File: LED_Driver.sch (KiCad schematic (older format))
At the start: 0 parts

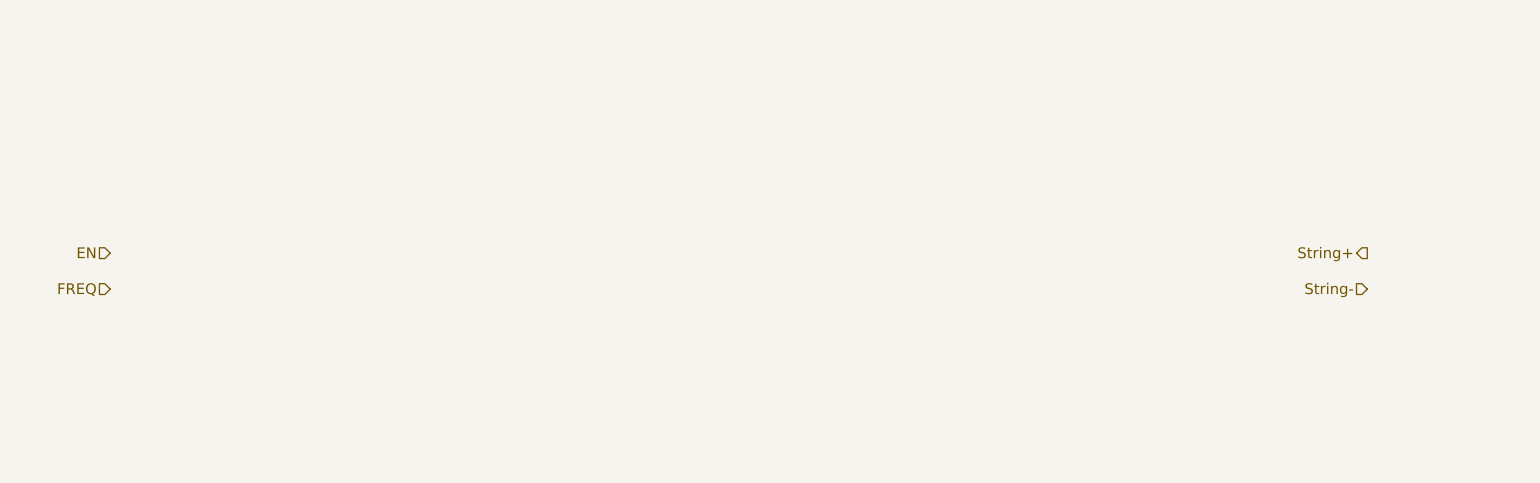
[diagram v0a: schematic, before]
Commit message: Rough schematic created for LED driver circuit
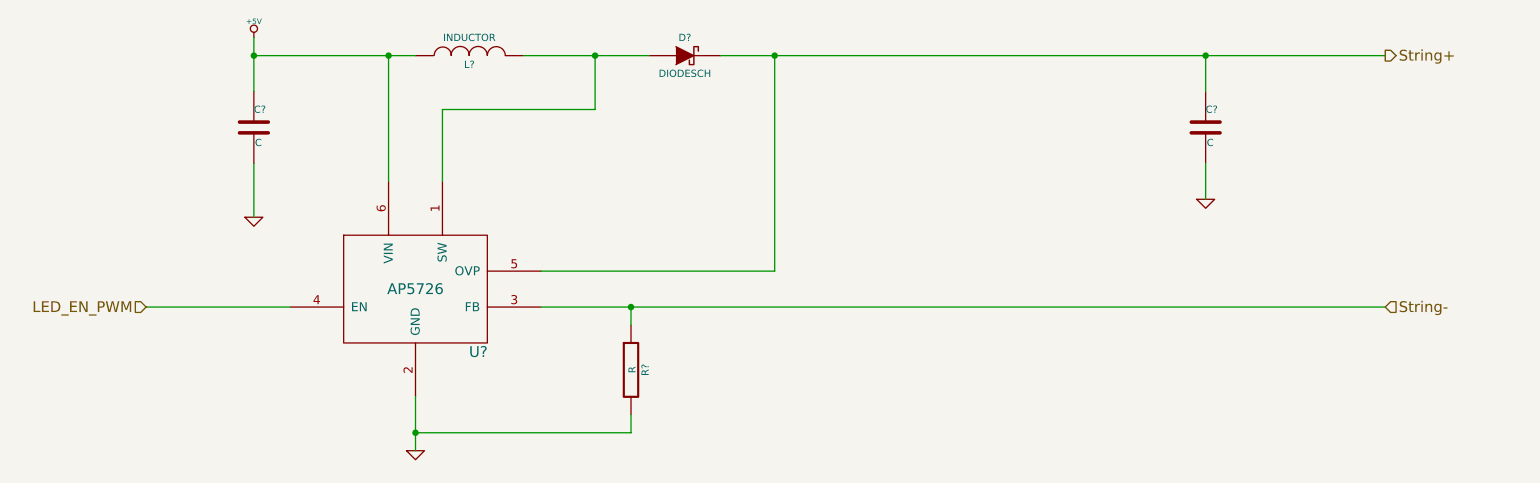
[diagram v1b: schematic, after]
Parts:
- added C? (x2): C, symbol C
- added D?: DIODESCH, symbol DIODESCH
- added L?: INDUCTOR, symbol INDUCTOR
- added R?: R, symbol R
- added U?: AP5726, symbol AP5726
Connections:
- net String+: now also C?.1, D?.2 (K), U?.5 (OVP)
- net String-: now also R?.1, U?.3 (FB)
- new net: D?.1 (A), L?.2, U?.1 (SW)
- new net +5V: C?.1, L?.1, U?.6 (VIN)
- new net GND: C?.2, C?.2, R?.2, U?.2 (GND)
- new net LED_EN_PWM: U?.4 (EN)
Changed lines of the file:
@@
 $Descr A4 11693 8268
 encoding utf-8
-Sheet 5 9
+Sheet 4 9
 Title ""
 Date ""
@@
 Comment4 ""
 $EndDescr
-Text HLabel 2400 2100 0    60   Input ~ 0
-EN
-Text HLabel 2400 2300 0    60   Input ~ 0
-FREQ
-Text HLabel 9400 2100 0    60   Output ~ 0
+Text HLabel 2600 2400 0    60   Input ~ 0
+LED_EN_PWM
+Text HLabel 9500 1000 2    60   Output ~ 0
 String+
-Text HLabel 9400 2300 0    60   Input ~ 0
+Text HLabel 9500 2400 2    60   Input ~ 0
 String-
+Wire Wire Line
+	2600 2400 3400 2400
+$Comp
+L AP5726 U?
+U 1 1 52F2B7AF
+P 4100 2300
+F 0 "U?" H 4450 1950 60  0000 C CNN
+F 1 "AP5726" H 4100 2300 60  0000 C CNN
+F 2 "" H 4100 2300 60  0000 C CNN
+F 3 "" H 4100 2300 60  0000 C CNN
+	1    4100 2300
+	1    0    0    -1
+$EndComp
+$Comp
+L +5V #PWR?
+U 1 1 52F2BDD5
+P 3200 900
+F 0 "#PWR?" H 3200 990 20  0001 C CNN
+F 1 "+5V" H 3200 990 30  0000 C CNN
+F 2 "" H 3200 900 60  0000 C CNN
+F 3 "" H 3200 900 60  0000 C CNN
+	1    3200 900
+	1    0    0    -1
+$EndComp
+$Comp
+L GND #PWR?
+U 1 1 52F2BDE9
+P 3200 1900
+F 0 "#PWR?" H 3200 1900 30  0001 C CNN
+F 1 "GND" H 3200 1830 30  0001 C CNN
+F 2 "" H 3200 1900 60  0000 C CNN
+F 3 "" H 3200 1900 60  0000 C CNN
+	1    3200 1900
+	1    0    0    -1
+$EndComp
+$Comp
+L GND #PWR?
+U 1 1 52F2BDFB
+P 4100 3200
+F 0 "#PWR?" H 4100 3200 30  0001 C CNN
+F 1 "GND" H 4100 3130 30  0001 C CNN
+F 2 "" H 4100 3200 60  0000 C CNN
+F 3 "" H 4100 3200 60  0000 C CNN
+	1    4100 3200
+	1    0    0    -1
+$EndComp
+Wire Wire Line
+	4100 3200 4100 2900
+$Comp
+L C C?
+U 1 1 52F2BE0B
+P 3200 1400
+F 0 "C?" H 3200 1500 40  0000 L CNN
+F 1 "C" H 3206 1315 40  0000 L CNN
+F 2 "" H 3238 1250 30  0000 C CNN
+F 3 "" H 3200 1400 60  0000 C CNN
+	1    3200 1400
+	1    0    0    -1
+$EndComp
+Wire Wire Line
+	3200 900  3200 1200
+Wire Wire Line
+	3200 1600 3200 1900
+Wire Wire Line
+	3950 1700 3950 1000
+Wire Wire Line
+	3200 1000 4100 1000
+Connection ~ 3200 1000
+$Comp
+L C C?
+U 1 1 52F2BE43
+P 8500 1400
+F 0 "C?" H 8500 1500 40  0000 L CNN
+F 1 "C" H 8506 1315 40  0000 L CNN
+F 2 "" H 8538 1250 30  0000 C CNN
+F 3 "" H 8500 1400 60  0000 C CNN
+	1    8500 1400
+	1    0    0    -1
+$EndComp
+$Comp
+L INDUCTOR L?
+U 1 1 52F2BE50
+P 4400 1000
+F 0 "L?" V 4350 1000 40  0000 C CNN
+F 1 "INDUCTOR" V 4500 1000 40  0000 C CNN
+F 2 "" H 4400 1000 60  0000 C CNN
+F 3 "" H 4400 1000 60  0000 C CNN
+	1    4400 1000
+	0    -1   -1   0
+$EndComp
+Connection ~ 3950 1000
+Wire Wire Line
+	4250 1700 4250 1300
+Wire Wire Line
+	4250 1300 5100 1300
+Wire Wire Line
+	5100 1300 5100 1000
+Wire Wire Line
+	4700 1000 5400 1000
+$Comp
+L DIODESCH D?
+U 1 1 52F2BE84
+P 5600 1000
+F 0 "D?" H 5600 1100 40  0000 C CNN
+F 1 "DIODESCH" H 5600 900 40  0000 C CNN
+F 2 "" H 5600 1000 60  0000 C CNN
+F 3 "" H 5600 1000 60  0000 C CNN
+	1    5600 1000
+	1    0    0    -1
+$EndComp
+Connection ~ 5100 1000
+Wire Wire Line
+	5800 1000 9500 1000
+Wire Wire Line
+	8500 1000 8500 1200
+$Comp
+L GND #PWR?
+U 1 1 52F2BEC8
+P 8500 1800
+F 0 "#PWR?" H 8500 1800 30  0001 C CNN
+F 1 "GND" H 8500 1730 30  0001 C CNN
+F 2 "" H 8500 1800 60  0000 C CNN
+F 3 "" H 8500 1800 60  0000 C CNN
+	1    8500 1800
+	1    0    0    -1
+$EndComp
+Wire Wire Line
+	8500 1800 8500 1600
+Connection ~ 8500 1000
+Wire Wire Line
+	4800 2400 9500 2400
+Wire Wire Line
+	5300 2400 5300 2500
+$Comp
+L R R?
+U 1 1 52F2BF1C
+P 5300 2750
+F 0 "R?" V 5380 2750 40  0000 C CNN
+F 1 "R" V 5307 2751 40  0000 C CNN
+F 2 "" V 5230 2750 30  0000 C CNN
+F 3 "" H 5300 2750 30  0000 C CNN
+	1    5300 2750
+	1    0    0    -1
+$EndComp
+Wire Wire Line
+	5300 3000 5300 3100
+Wire Wire Line
+	5300 3100 4100 3100
+Connection ~ 4100 3100
+Connection ~ 5300 2400
+Wire Wire Line
+	4800 2200 6100 2200
+Wire Wire Line
+	6100 2200 6100 1000
+Connection ~ 6100 1000
 $EndSCHEMATC

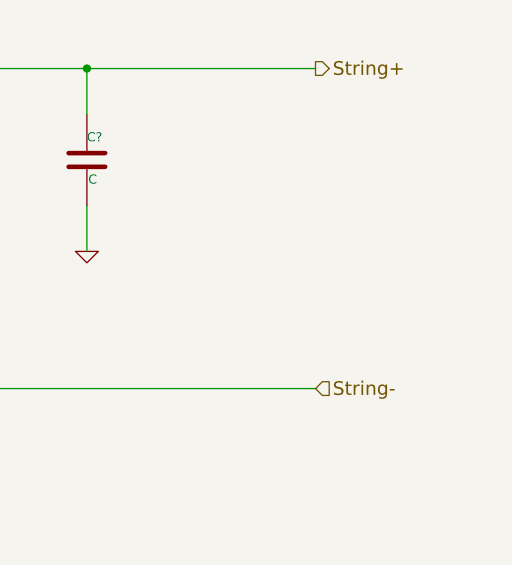
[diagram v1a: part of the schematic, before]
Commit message: Added Arduino and top-level connections
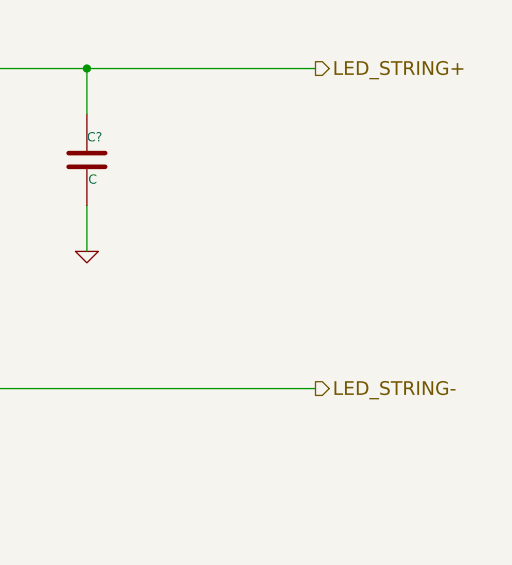
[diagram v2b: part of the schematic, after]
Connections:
- net String+ renamed LED_STRING+
- net String- renamed LED_STRING-
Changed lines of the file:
@@
 LED_EN_PWM
 Text HLabel 9500 1000 2    60   Output ~ 0
-String+
-Text HLabel 9500 2400 2    60   Input ~ 0
-String-
+LED_STRING+
+Text HLabel 9500 2400 2    60   Output ~ 0
+LED_STRING-
 Wire Wire Line
 	2600 2400 3400 2400

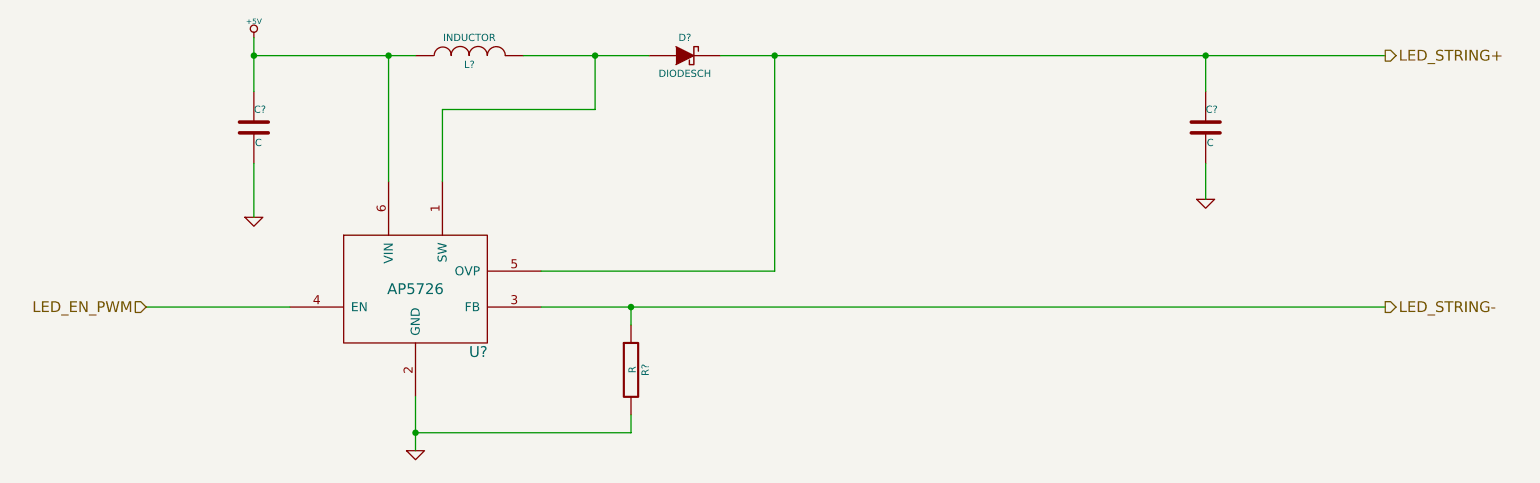
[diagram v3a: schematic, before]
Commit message: Added footprints for the relay module, preliminarily annotated schematic, relay components placed on PCB
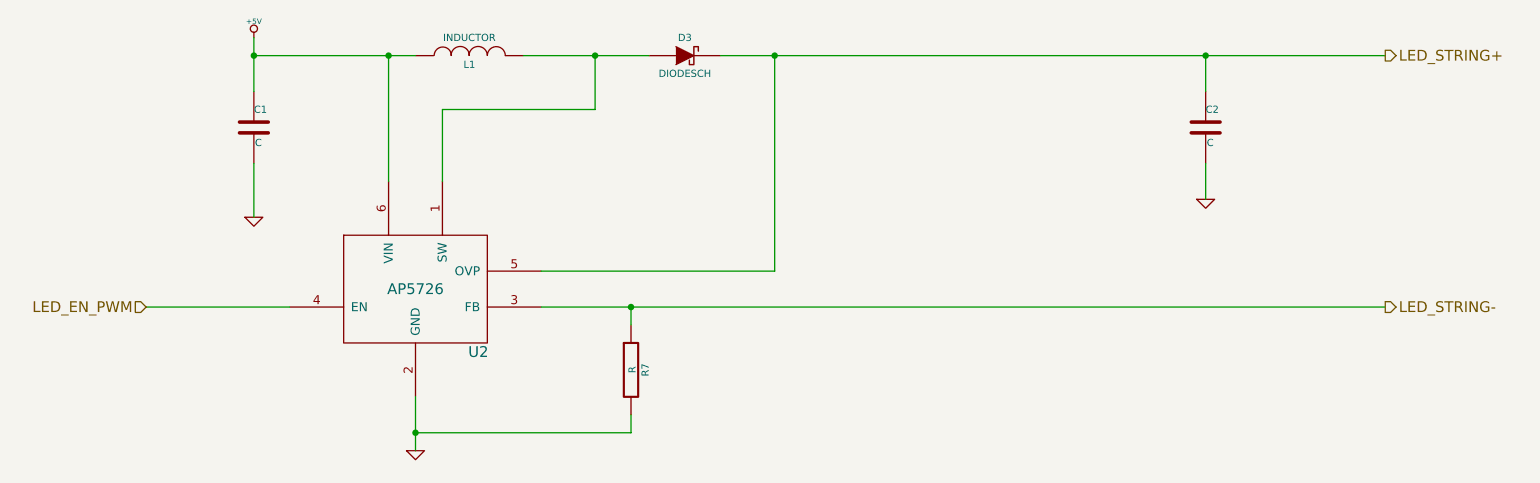
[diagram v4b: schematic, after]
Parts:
- gave numbers to parts that had none: 6
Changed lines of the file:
@@
 	2600 2400 3400 2400
 $Comp
-L AP5726 U?
+L AP5726 U2
 U 1 1 52F2B7AF
 P 4100 2300
-F 0 "U?" H 4450 1950 60  0000 C CNN
+F 0 "U2" H 4450 1950 60  0000 C CNN
 F 1 "AP5726" H 4100 2300 60  0000 C CNN
 F 2 "" H 4100 2300 60  0000 C CNN
@@
 $EndComp
 $Comp
-L +5V #PWR?
+L +5V #PWR3
 U 1 1 52F2BDD5
 P 3200 900
-F 0 "#PWR?" H 3200 990 20  0001 C CNN
+F 0 "#PWR3" H 3200 990 20  0001 C CNN
 F 1 "+5V" H 3200 990 30  0000 C CNN
 F 2 "" H 3200 900 60  0000 C CNN
@@
 $EndComp
 $Comp
-L GND #PWR?
+L GND #PWR4
 U 1 1 52F2BDE9
 P 3200 1900
-F 0 "#PWR?" H 3200 1900 30  0001 C CNN
+F 0 "#PWR4" H 3200 1900 30  0001 C CNN
 F 1 "GND" H 3200 1830 30  0001 C CNN
 F 2 "" H 3200 1900 60  0000 C CNN
@@
 $EndComp
 $Comp
-L GND #PWR?
+L GND #PWR5
 U 1 1 52F2BDFB
 P 4100 3200
-F 0 "#PWR?" H 4100 3200 30  0001 C CNN
+F 0 "#PWR5" H 4100 3200 30  0001 C CNN
 F 1 "GND" H 4100 3130 30  0001 C CNN
 F 2 "" H 4100 3200 60  0000 C CNN
@@
 	4100 3200 4100 2900
 $Comp
-L C C?
+L C C1
 U 1 1 52F2BE0B
 P 3200 1400
-F 0 "C?" H 3200 1500 40  0000 L CNN
+F 0 "C1" H 3200 1500 40  0000 L CNN
 F 1 "C" H 3206 1315 40  0000 L CNN
 F 2 "" H 3238 1250 30  0000 C CNN
@@
 Connection ~ 3200 1000
 $Comp
-L C C?
+L C C2
 U 1 1 52F2BE43
 P 8500 1400
-F 0 "C?" H 8500 1500 40  0000 L CNN
+F 0 "C2" H 8500 1500 40  0000 L CNN
 F 1 "C" H 8506 1315 40  0000 L CNN
 F 2 "" H 8538 1250 30  0000 C CNN
@@
 $EndComp
 $Comp
-L INDUCTOR L?
+L INDUCTOR L1
 U 1 1 52F2BE50
 P 4400 1000
-F 0 "L?" V 4350 1000 40  0000 C CNN
+F 0 "L1" V 4350 1000 40  0000 C CNN
 F 1 "INDUCTOR" V 4500 1000 40  0000 C CNN
 F 2 "" H 4400 1000 60  0000 C CNN
@@
 	4700 1000 5400 1000
 $Comp
-L DIODESCH D?
+L DIODESCH D3
 U 1 1 52F2BE84
 P 5600 1000
-F 0 "D?" H 5600 1100 40  0000 C CNN
+F 0 "D3" H 5600 1100 40  0000 C CNN
 F 1 "DIODESCH" H 5600 900 40  0000 C CNN
 F 2 "" H 5600 1000 60  0000 C CNN
@@
 	8500 1000 8500 1200
 $Comp
-L GND #PWR?
+L GND #PWR6
 U 1 1 52F2BEC8
 P 8500 1800
-F 0 "#PWR?" H 8500 1800 30  0001 C CNN
+F 0 "#PWR6" H 8500 1800 30  0001 C CNN
 F 1 "GND" H 8500 1730 30  0001 C CNN
 F 2 "" H 8500 1800 60  0000 C CNN
@@
 	5300 2400 5300 2500
 $Comp
-L R R?
+L R R7
 U 1 1 52F2BF1C
 P 5300 2750
-F 0 "R?" V 5380 2750 40  0000 C CNN
+F 0 "R7" V 5380 2750 40  0000 C CNN
 F 1 "R" V 5307 2751 40  0000 C CNN
 F 2 "" V 5230 2750 30  0000 C CNN

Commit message: Associated and placed the LED Driver Module
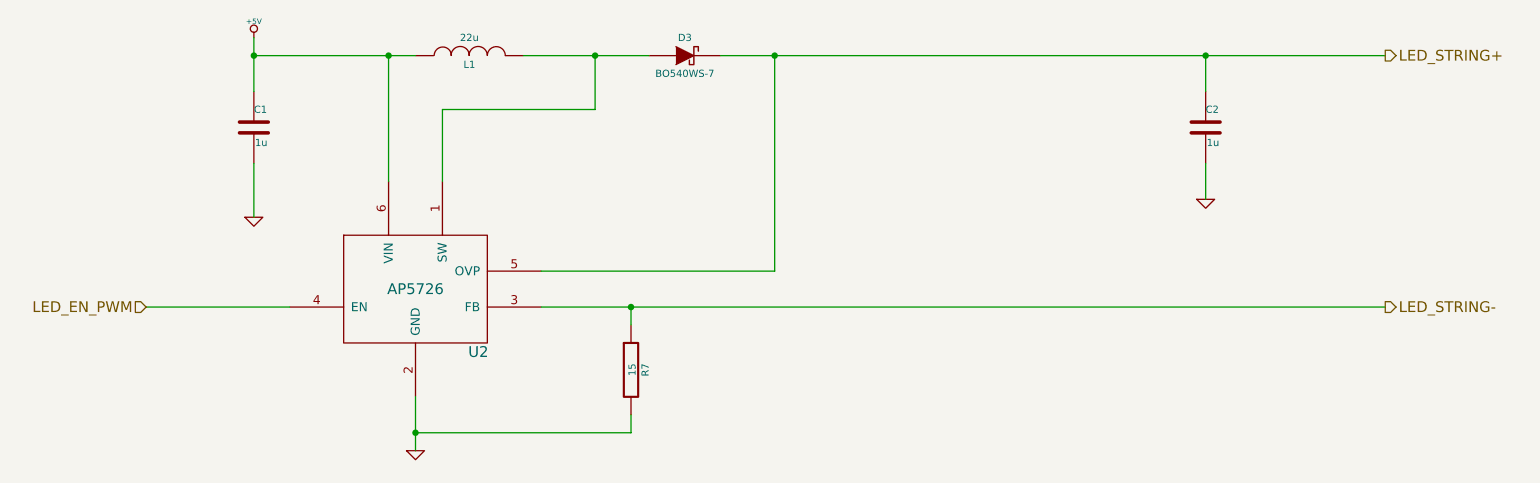
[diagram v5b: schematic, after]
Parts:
- C1, C2: value C -> 1u
- D3: value DIODESCH -> BO540WS-7; MFG Part Number (none) -> BO540WS-7
- L1: value INDUCTOR -> 22u; MFG Part Number (none) -> NR4012T220M
- R7: value R -> 15
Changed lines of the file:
@@
 $EndComp
 $Comp
-L +5V #PWR3
+L +5V #PWR03
 U 1 1 52F2BDD5
 P 3200 900
-F 0 "#PWR3" H 3200 990 20  0001 C CNN
+F 0 "#PWR03" H 3200 990 20  0001 C CNN
 F 1 "+5V" H 3200 990 30  0000 C CNN
 F 2 "" H 3200 900 60  0000 C CNN
@@
 $EndComp
 $Comp
-L GND #PWR4
+L GND #PWR04
 U 1 1 52F2BDE9
 P 3200 1900
-F 0 "#PWR4" H 3200 1900 30  0001 C CNN
+F 0 "#PWR04" H 3200 1900 30  0001 C CNN
 F 1 "GND" H 3200 1830 30  0001 C CNN
 F 2 "" H 3200 1900 60  0000 C CNN
@@
 $EndComp
 $Comp
-L GND #PWR5
+L GND #PWR05
 U 1 1 52F2BDFB
 P 4100 3200
-F 0 "#PWR5" H 4100 3200 30  0001 C CNN
+F 0 "#PWR05" H 4100 3200 30  0001 C CNN
 F 1 "GND" H 4100 3130 30  0001 C CNN
 F 2 "" H 4100 3200 60  0000 C CNN
@@
 P 3200 1400
 F 0 "C1" H 3200 1500 40  0000 L CNN
-F 1 "C" H 3206 1315 40  0000 L CNN
+F 1 "1u" H 3206 1315 40  0000 L CNN
 F 2 "" H 3238 1250 30  0000 C CNN
 F 3 "" H 3200 1400 60  0000 C CNN
@@
 P 8500 1400
 F 0 "C2" H 8500 1500 40  0000 L CNN
-F 1 "C" H 8506 1315 40  0000 L CNN
+F 1 "1u" H 8506 1315 40  0000 L CNN
 F 2 "" H 8538 1250 30  0000 C CNN
 F 3 "" H 8500 1400 60  0000 C CNN
@@
 P 4400 1000
 F 0 "L1" V 4350 1000 40  0000 C CNN
-F 1 "INDUCTOR" V 4500 1000 40  0000 C CNN
+F 1 "22u" V 4500 1000 40  0000 C CNN
 F 2 "" H 4400 1000 60  0000 C CNN
 F 3 "" H 4400 1000 60  0000 C CNN
+F 4 "NR4012T220M" H 4400 1000 60  0001 C CNN "MFG Part Number"
 	1    4400 1000
 	0    -1   -1   0
@@
 P 5600 1000
 F 0 "D3" H 5600 1100 40  0000 C CNN
-F 1 "DIODESCH" H 5600 900 40  0000 C CNN
+F 1 "BO540WS-7" H 5600 900 40  0000 C CNN
 F 2 "" H 5600 1000 60  0000 C CNN
 F 3 "" H 5600 1000 60  0000 C CNN
+F 4 "BO540WS-7" H 5600 1000 60  0001 C CNN "MFG Part Number"
 	1    5600 1000
 	1    0    0    -1
@@
 	8500 1000 8500 1200
 $Comp
-L GND #PWR6
+L GND #PWR06
 U 1 1 52F2BEC8
 P 8500 1800
-F 0 "#PWR6" H 8500 1800 30  0001 C CNN
+F 0 "#PWR06" H 8500 1800 30  0001 C CNN
 F 1 "GND" H 8500 1730 30  0001 C CNN
 F 2 "" H 8500 1800 60  0000 C CNN
@@
 P 5300 2750
 F 0 "R7" V 5380 2750 40  0000 C CNN
-F 1 "R" V 5307 2751 40  0000 C CNN
+F 1 "15" V 5307 2751 40  0000 C CNN
 F 2 "" V 5230 2750 30  0000 C CNN
 F 3 "" H 5300 2750 30  0000 C CNN

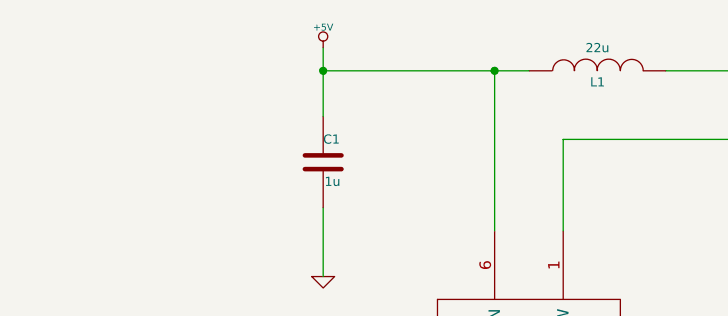
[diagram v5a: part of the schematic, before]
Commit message: Various minor updates after Ground and Power Planes video
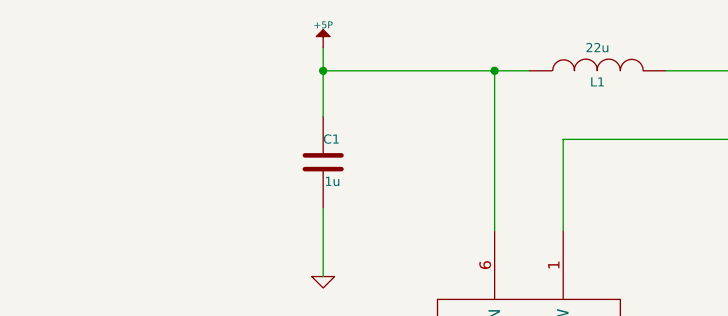
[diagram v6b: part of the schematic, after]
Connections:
- net +5V renamed +5P
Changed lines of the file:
@@
 $EndComp
 $Comp
-L +5V #PWR03
-U 1 1 52F2BDD5
-P 3200 900
-F 0 "#PWR03" H 3200 990 20  0001 C CNN
-F 1 "+5V" H 3200 990 30  0000 C CNN
-F 2 "" H 3200 900 60  0000 C CNN
-F 3 "" H 3200 900 60  0000 C CNN
-	1    3200 900
-	1    0    0    -1
-$EndComp
-$Comp
-L GND #PWR04
+L GND #PWR4
 U 1 1 52F2BDE9
 P 3200 1900
-F 0 "#PWR04" H 3200 1900 30  0001 C CNN
+F 0 "#PWR4" H 3200 1900 30  0001 C CNN
 F 1 "GND" H 3200 1830 30  0001 C CNN
 F 2 "" H 3200 1900 60  0000 C CNN
@@
 $EndComp
 $Comp
-L GND #PWR05
+L GND #PWR5
 U 1 1 52F2BDFB
 P 4100 3200
-F 0 "#PWR05" H 4100 3200 30  0001 C CNN
+F 0 "#PWR5" H 4100 3200 30  0001 C CNN
 F 1 "GND" H 4100 3130 30  0001 C CNN
 F 2 "" H 4100 3200 60  0000 C CNN
@@
 	8500 1000 8500 1200
 $Comp
-L GND #PWR06
+L GND #PWR6
 U 1 1 52F2BEC8
 P 8500 1800
-F 0 "#PWR06" H 8500 1800 30  0001 C CNN
+F 0 "#PWR6" H 8500 1800 30  0001 C CNN
 F 1 "GND" H 8500 1730 30  0001 C CNN
 F 2 "" H 8500 1800 60  0000 C CNN
@@
 	6100 2200 6100 1000
 Connection ~ 6100 1000
+$Comp
+L +5P #PWR3
+U 1 1 5314D93E
+P 3200 900
+F 0 "#PWR3" H 3200 1030 20  0001 C CNN
+F 1 "+5P" H 3200 1000 30  0000 C CNN
+F 2 "" H 3200 900 60  0000 C CNN
+F 3 "" H 3200 900 60  0000 C CNN
+	1    3200 900
+	1    0    0    -1
+$EndComp
 $EndSCHEMATC
